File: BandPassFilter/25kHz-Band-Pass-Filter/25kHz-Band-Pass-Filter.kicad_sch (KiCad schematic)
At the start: 19 parts, among them J1 Conn_01x02, U1 ${SIM.PARAMS}, U2 ${SIM.PARAMS}, U3 ${SIM.PARAMS}, U4 MCP6S21-I_SN

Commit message: Expanded hydrophone board
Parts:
- added C10, C9: 5.1nF, Capacitor_THT:CP_Axial_L10.0mm_D4.5mm_P15.00mm_Horizontal, symbol Device:C
- added C11, C12: 4.7nF, Capacitor_THT:CP_Axial_L10.0mm_D4.5mm_P15.00mm_Horizontal, symbol Device:C
- added C13, C14: 4.4nF, Capacitor_THT:CP_Axial_L10.0mm_D4.5mm_P15.00mm_Horizontal, symbol Device:C
- added C15, C16: 4.1nF, Capacitor_THT:CP_Axial_L10.0mm_D4.5mm_P15.00mm_Horizontal, symbol Device:C
- added C17, C18: 3.9nF, Capacitor_THT:CP_Axial_L10.0mm_D4.5mm_P15.00mm_Horizontal, symbol Device:C
- added C7, C8: 5.5nF, Capacitor_THT:CP_Axial_L10.0mm_D4.5mm_P15.00mm_Horizontal, symbol Device:C
- added J2, J3, J4: Conn_01x02, Connector_Coaxial:BNC_Amphenol_031-5539_Vertical, symbol Connector_Generic:Conn_01x02
- added R10, R13, R14, R17, R18, R21, R22, R25, R26, R29, R30, R9: 1kΩ, Resistor_THT:R_Axial_DIN0204_L3.6mm_D1.6mm_P1.90mm_Vertical, symbol Device:R
- added R11, R15, R19, R23, R27, R31: 100kΩ, Resistor_THT:R_Axial_DIN0204_L3.6mm_D1.6mm_P1.90mm_Vertical, symbol Device:R
- added R12, R16, R20, R24, R28, R32: 1MΩ, Resistor_THT:R_Axial_DIN0204_L3.6mm_D1.6mm_P1.90mm_Vertical, symbol Device:R
- added U10, U11, U12, U13, U5, U6, U7, U8, U9: ${SIM.PARAMS}, Package_SO:SOIC-8-1EP_3.9x4.9mm_P1.27mm_EP2.29x3mm, symbol Simulation_SPICE:OPAMP
- added U14: LTC2171CUKG-14_PBF, LTC2171CUKG-14_PBF:QFN50P700X800X80-53N, symbol CUSTOM ADC:LTC2171CUKG-14_PBF
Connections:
- net +5V: now also C1.2, J1.2 (Pin_2), U4.1 (VOUT), C11.2, C15.2, C7.2, J2.2 (Pin_2), J3.2 (Pin_2), J4.2 (Pin_2), U10.3 (V+), U11.3 (V+), U12.3 (V+), U13.3 (V+), U5.3 (V+), U6.3 (V+), U7.3 (V+), U8.3 (V+), U9.3 (V+)
- net -5V: now also U10.4 (V-), U11.4 (V-), U12.4 (V-), U13.4 (V-), U5.4 (V-), U6.4 (V-), U7.4 (V-), U8.4 (V-), U9.4 (V-)
- net GND: now also C10.2, C14.2, C18.2, J2.1 (Pin_1), J3.1 (Pin_1), J4.1 (Pin_1), R10.2, R11.2, R15.1, R18.2, R19.2, R23.1, R26.2, R27.2, R31.1, U14.11 (AIN3-), U14.14 (AIN4-), U14.19 (~CS), U14.2 (AIN1-), U14.22 (GND_2), U14.33 (OGND), U14.45 (GND_3), U14.49 (GND), U14.5 (AIN2-), U14.53 (EP)
- net VOUT: no longer names the net of C3.1, R8.1, U3.5
- net VOUT: now also U14.1 (AIN1+)
- new net: C15.1, C16.2, R25.2
- new net: C8.1, R10.1, U5.1 (+)
- new net: C7.1, C8.2, R9.2
- new net: C12.1, R18.1, U8.1 (+)
- new net: C9.1, R16.1, U14.4 (AIN2+), U7.5
- new net: C9.2, R13.1, R14.2
- new net: C16.1, R26.1, U11.1 (+)
- new net: R27.1, R28.2, U11.2 (-)
- new net: R25.1, R28.1, U11.5, U12.1 (+)
- new net: R29.2, U12.2 (-), U12.5
- new net: C13.1, R24.1, U10.5, U14.10 (AIN3+)
- new net: C17.1, R32.1, U13.5, U14.13 (AIN4+)
- new net: C18.1, R30.1, U13.1 (+)
- new net: R31.2, R32.2, U13.2 (-)
- new net: R15.2, R16.2, U7.2 (-)
- new net: R23.2, R24.2, U10.2 (-)
- new net: C13.2, R21.1, R22.2
- new net: R11.1, R12.2, U5.2 (-)
- new net: R12.1, R9.1, U5.5, U6.1 (+)
- new net: C17.2, R29.1, R30.2
- new net: R17.1, R20.1, U8.5, U9.1 (+)
- new net: C11.1, C12.2, R17.2
- new net: R21.2, U9.2 (-), U9.5
- new net: C14.1, R22.1, U10.1 (+)
- new net: C10.1, R14.1, U7.1 (+)
- new net: R19.1, R20.2, U8.2 (-)
- new net: R13.2, U6.2 (-), U6.5
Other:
- note added: "ADC Converter"
- note added: "Band Pass 25kHz"
- note added: "Band Pass 30kHz"
- note added: "Band Pass 35kHz"
- note added: "Band Pass 40kHz"
- note removed: "Band Pass"
- moved on the sheet: C1, C2, C3, C4, C5, C6, J1, R1, R2, R3, R4, R5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

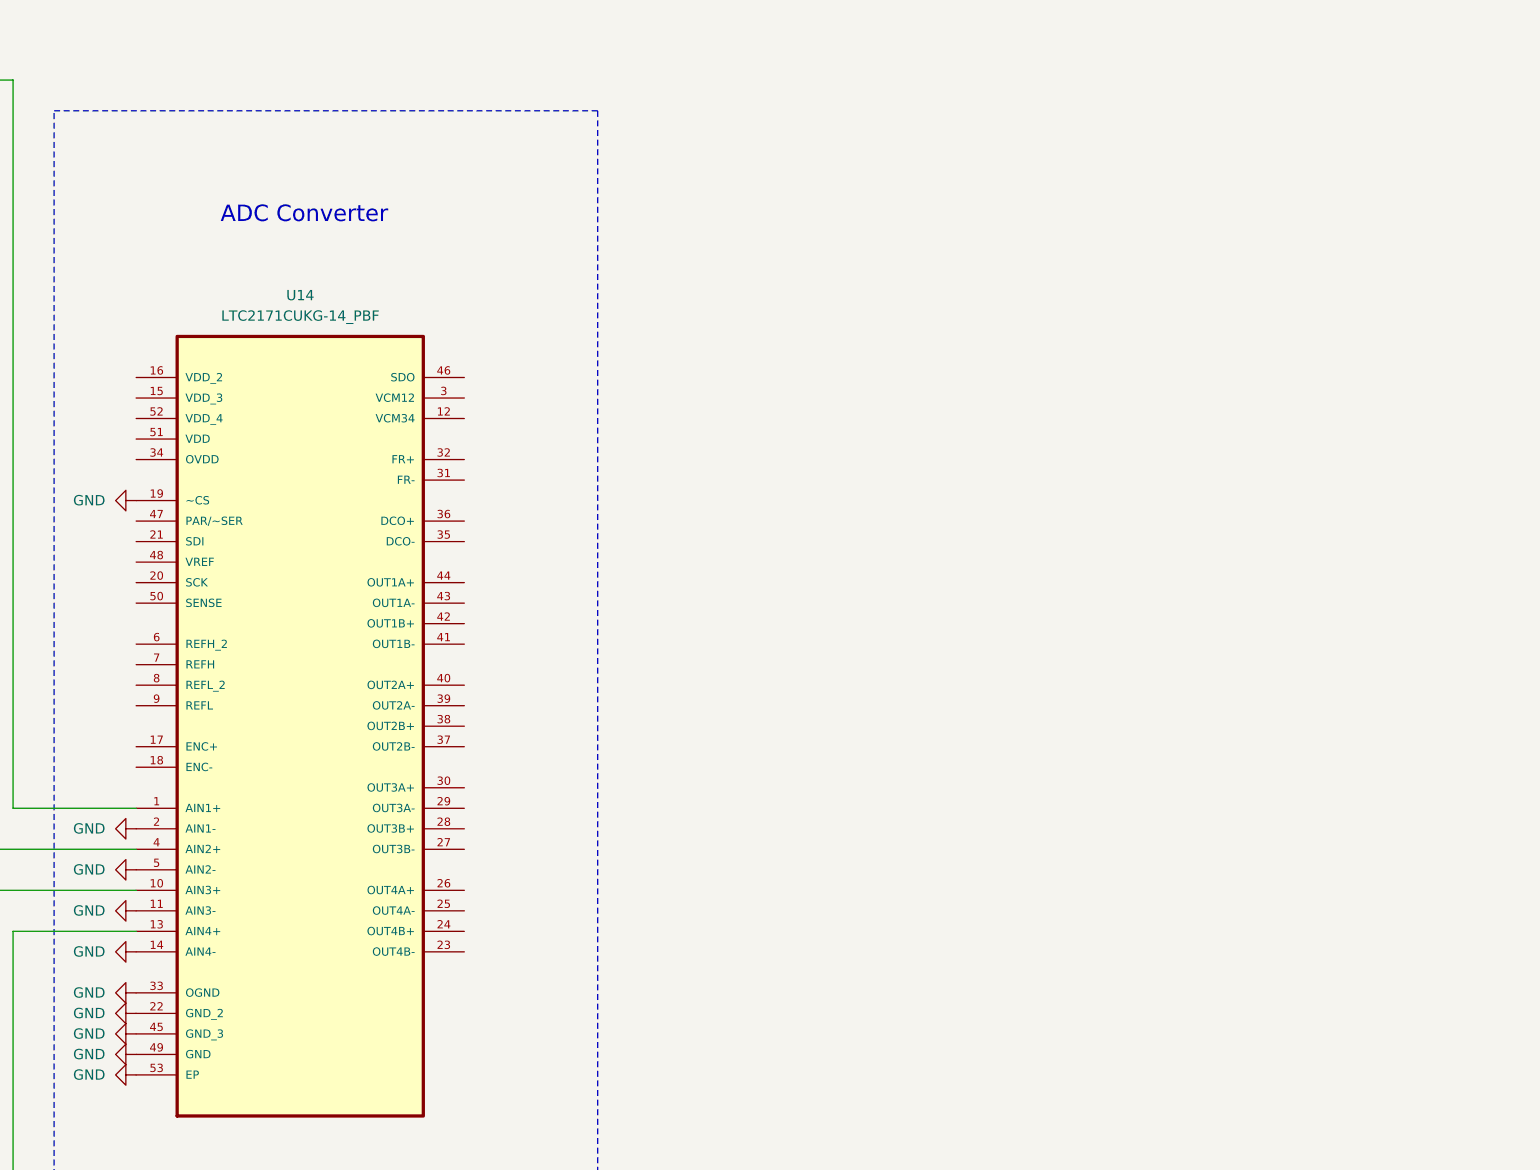
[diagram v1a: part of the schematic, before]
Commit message: added footprint for LVDS and added pins for esp
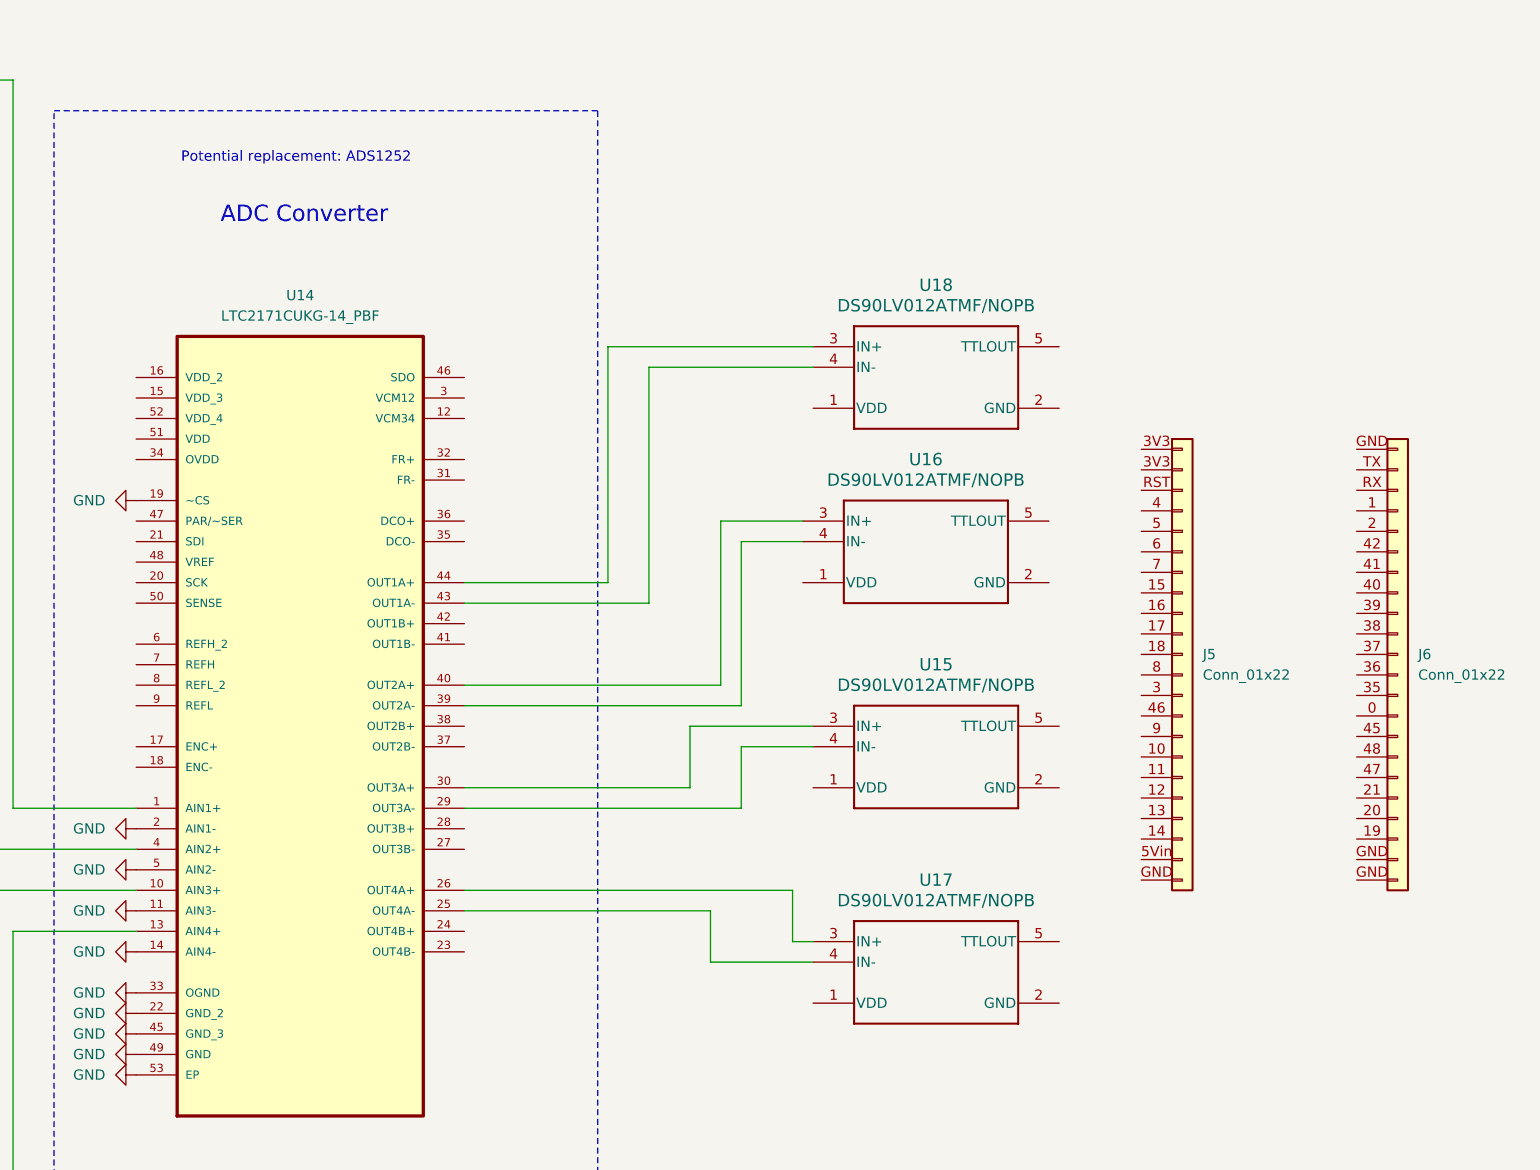
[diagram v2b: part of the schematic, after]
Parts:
- added J5, J6: Conn_01x22, symbol Connector_Generic:Conn_01x22
- added U15: DS90LV012ATMF/NOPB, DS90LV012ATMF-NOPB:DS90LV012ATMF-NOPB, symbol DS90LV012ATMF-NOPB:DS90LV012ATMF_NOPB
- added U16, U17, U18: DS90LV012ATMF/NOPB, MF05A_N, symbol DS90LV012ATMF-NOPB:DS90LV012ATMF_NOPB
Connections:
- net at U14.25 (OUT4A-): now also U17.4 (IN-)
- net at U14.26 (OUT4A+): now also U17.3 (IN+)
- net at U14.29 (OUT3A-): now also U15.4 (IN-)
- net at U14.30 (OUT3A+): now also U15.3 (IN+)
- net at U14.39 (OUT2A-): now also U16.4 (IN-)
- net at U14.40 (OUT2A+): now also U16.3 (IN+)
- net at U14.43 (OUT1A-): now also U18.4 (IN-)
- net at U14.44 (OUT1A+): now also U18.3 (IN+)
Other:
- note added: "Potential replacement: ADS1252"

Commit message: completed_board
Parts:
- removed U14: LTC2171CUKG-14_PBF, LTC2171CUKG-14_PBF:QFN50P700X800X80-53N, symbol CUSTOM ADC:LTC2171CUKG-14_PBF
- removed U15: DS90LV012ATMF/NOPB, DS90LV012ATMF-NOPB:DS90LV012ATMF-NOPB, symbol DS90LV012ATMF-NOPB:DS90LV012ATMF_NOPB
- removed U16, U17, U18: DS90LV012ATMF/NOPB, MF05A_N, symbol DS90LV012ATMF-NOPB:DS90LV012ATMF_NOPB
- added C19, C20, C23, C25, C27, C29, C31, C33: 22u, symbol Device:C
- added C21, C22, C24, C26, C28, C30, C32, C34: C, symbol Device:C
- added R33, R37, R41, R45: 20k, symbol Device:R
- added R34, R36, R38, R39, R42, R43, R46, R47: 10k, symbol Device:R
- added R35, R40, R44, R48: 5k, symbol Device:R
- added U14, U15, U16, U17: ADS1252, Package_SO:SOIC-8_3.9x4.9mm_P1.27mm, symbol Analog_ADC:ADS1251
- added U18, U19, U20, U21, U22, U23, U24, U25, U26, U27, U28, U29: OPA4350, Package_SO:SOIC-8_3.9x4.9mm_P1.27mm, symbol Amplifier_Operational:OPA340UA
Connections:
- net +5V: now also J5.5Vin (Pin_21), U14.3 (VCC), U15.3 (VCC), U16.3 (VCC), U17.3 (VCC); no longer C1.2, C11.2, C15.2, C7.2, J1.2 (Pin_2), J2.2 (Pin_2), J3.2 (Pin_2), J4.2 (Pin_2), U4.1 (VOUT)
- net GND: now also J5.GND (Pin_22), J6.GND (Pin_22), C19.1, C20.2, C21.1, C22.2, C23.1, C24.1, C25.2, C26.2, C27.1, C28.1, C29.2, C30.2, C31.1, C32.1, C33.2, C34.2, R34.1, R38.1, R42.1, R46.1, U15.7 (GND), U16.7 (GND), U17.7 (GND)
- net at C9.1, R16.1, U7.5: now also R37.1
- net at C3.1, R8.1, U3.5: now also R33.1
- net at C13.1, R24.1, U10.5: now also R41.1
- net at C17.1, R32.1, U13.5: now also R45.1
- net at J5.10 (Pin_16): now also U16.5 (DOUT/nDRDY)
- net at J5.11 (Pin_17): now also U17.5 (DOUT/nDRDY)
- net +3V3: now reaches J5.3V3 (Pin_2)
- net +3V3: now also U19.3 (+), U20.3 (+), U21.3 (+), U23.3 (+), U24.3 (+), U26.3 (+), U27.3 (+), U29.3 (+)
- net at J5.6 (Pin_6): now also U14.4 (CLK), U14.6 (SCLK), U15.4 (CLK), U15.6 (SCLK), U16.4 (CLK), U16.6 (SCLK), U17.4 (CLK), U17.6 (SCLK)
- net at J5.8 (Pin_12): now also U14.5 (DOUT/nDRDY)
- net at J5.9 (Pin_15): now also U15.5 (DOUT/nDRDY)
- new net: C32.2, C34.1, U17.8 (VREF), U29.2 (-), U29.6
- new net: C1.2, C11.2, C15.2, C7.2, J1.2 (Pin_2), J2.2 (Pin_2), J3.2 (Pin_2), J4.2 (Pin_2), U4.1 (VOUT)
- new net: R35.2, U14.1 (IN+), U18.6
- new net: C19.2, C20.1, R36.1, U14.2 (IN-), U19.2 (-), U19.6
- new net: C21.2, C22.1, U14.8 (VREF), U20.2 (-), U20.6
- new net: R42.2, R44.1, U25.2 (-)
- new net: R44.2, U16.1 (IN+), U25.6
- new net: C23.2, C25.1, R39.1, U15.2 (IN-), U21.2 (-), U21.6
- new net: R38.2, R40.1, U22.2 (-)
- new net: R37.2, R39.2, U22.3 (+)
- new net: R40.2, U15.1 (IN+), U22.6
- new net: R41.2, R43.2, U25.3 (+)
- new net: C24.2, C26.1, U15.8 (VREF), U23.2 (-), U23.6
- new net: C31.2, C33.1, R47.1, U17.2 (IN-), U27.2 (-), U27.6
- new net: C27.2, C29.1, R43.1, U16.2 (IN-), U24.2 (-), U24.6
- new net: R33.2, R36.2, U18.3 (+)
- new net: R46.2, R48.1, U28.2 (-)
- new net: R48.2, U17.1 (IN+), U28.6
- new net: C28.2, C30.1, U16.8 (VREF), U26.2 (-), U26.6
- new net: R34.2, R35.1, U18.2 (-)
- new net: R45.2, R47.2, U28.3 (+)
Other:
- note removed: "ADC Converter"
- note removed: "Potential replacement: ADS1252"
